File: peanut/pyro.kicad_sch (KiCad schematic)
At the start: 16 parts, among them J2 PYRO_OUT, Q2 NMOS, Q3 NMOS, Q4 NMOS

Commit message: bug: Fix arming flaw
Fixed the arming circuitry so that the ARM terminal prevents power going
to the pyro channels. This means that the rest of the board can be
powered on before arming, which is good because:

- It allows configuring without arming
- Software arming can still be done as a second stage
- The MCU can be in low-power mode until told to arm over BLE
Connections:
- net VBAT_RAW renamed VPYRO
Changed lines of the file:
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@@
 		(in_pos_files yes)
 		(dnp no)
-		(fields_autoplaced yes)
 		(property "Reference" "#PWR058"
 			(at 196.85 93.98 0)
@@
 			)
 		)
-		(property "Value" "VBAT_RAW"
-			(at 196.85 85.09 0)
-			(show_name no)
-			(do_not_autoplace no)
-			(effects
-				(font
-					(size 1.27 1.27)
-				)
+		(property "Value" "VPYRO"
+			(at 194.056 85.598 0)
+			(show_name no)
+			(do_not_autoplace no)
+			(effects
+				(font
+					(size 1.27 1.27)
+				)
+				(justify left)
 			)
 		)
@@
 		(in_pos_files yes)
 		(dnp no)
-		(fields_autoplaced yes)
 		(property "Reference" "#PWR057"
 			(at 156.21 93.98 0)
@@
 			)
 		)
-		(property "Value" "VBAT_RAW"
-			(at 156.21 85.09 0)
-			(show_name no)
-			(do_not_autoplace no)
-			(effects
-				(font
-					(size 1.27 1.27)
-				)
-			)
-		)
+		(property "Value" "VPYRO"
+			(at 153.67 85.598 0)
+			(show_name no)
+			(do_not_autoplace no)
+			(effects
+				(font
+					(size 1.27 1.27)
+				)
+				(justify left)
+			)
+		)

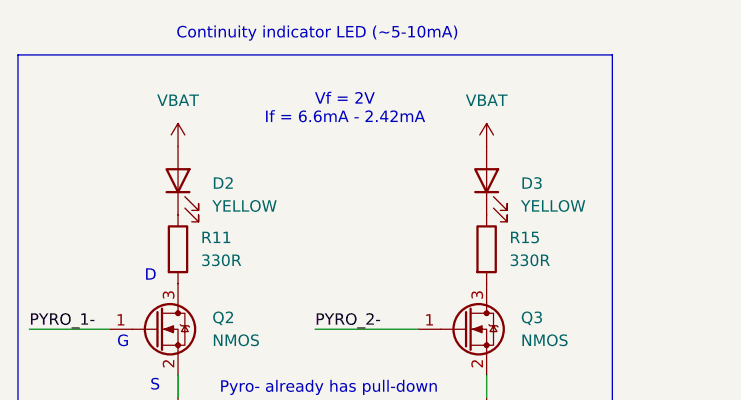
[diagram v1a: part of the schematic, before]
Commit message: chore: Clean up routing
Cleaned up some traces and added teardrops.
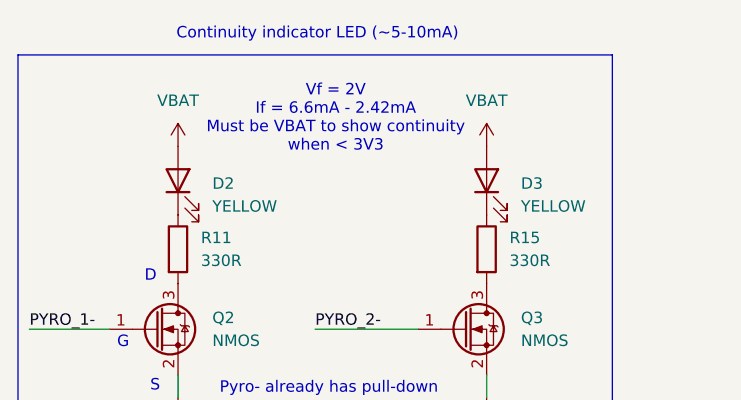
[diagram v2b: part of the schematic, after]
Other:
- note added: "Vf = 2V If = 6.6mA - 2.42mA Must be VBAT to show continuity when < 3V3"
- note removed: "Vf = 2V If = 6.6mA - 2.42mA"
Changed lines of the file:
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@@
 		)
 	)
-	(text "Vf = 2V\nIf = 6.6mA - 2.42mA"
+	(text "Vf = 2V\nIf = 6.6mA - 2.42mA\nMust be VBAT to show continuity\nwhen < 3V3"
 		(exclude_from_sim no)
-		(at 69.342 88.646 0)
+		(at 68.326 89.662 0)
 		(effects
 			(font

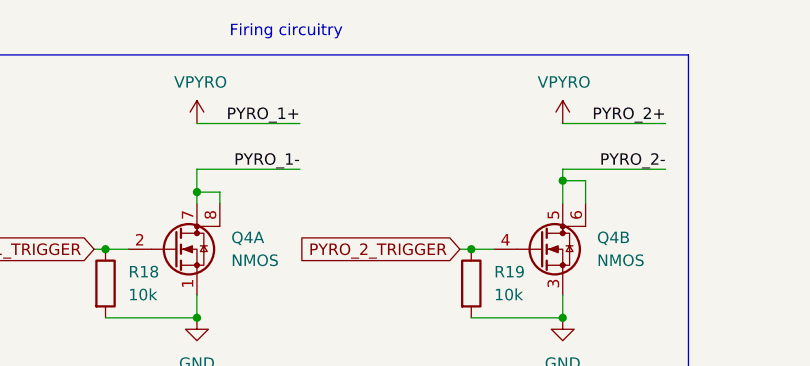
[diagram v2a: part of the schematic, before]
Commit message: feat: Better arming circuit
Improved the arming circuit connections so that both circuits are
powered off until armed.

Signed-off-by: Matteo Golin <matteo.golin@gmail.com>
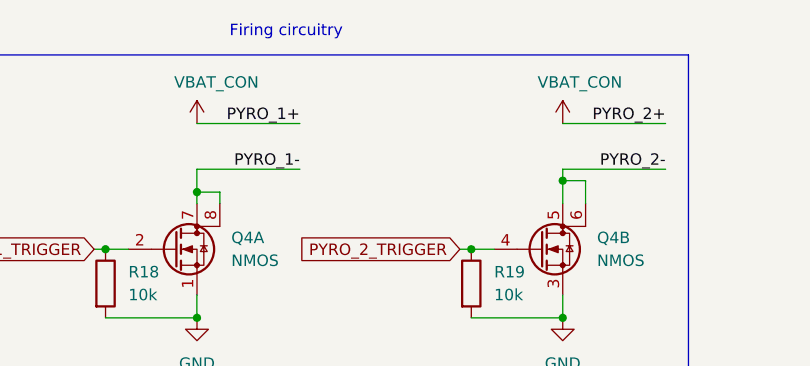
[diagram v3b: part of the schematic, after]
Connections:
- net VPYRO renamed VBAT_CON
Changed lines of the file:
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@@
 			)
 		)
-		(property "Value" "VPYRO"
+		(property "Value" "VBAT_CON"
 			(at 194.056 85.598 0)
 			(show_name no)
@@
 			)
 		)
-		(property "Value" "VPYRO"
+		(property "Value" "VBAT_CON"
 			(at 153.67 85.598 0)
 			(show_name no)

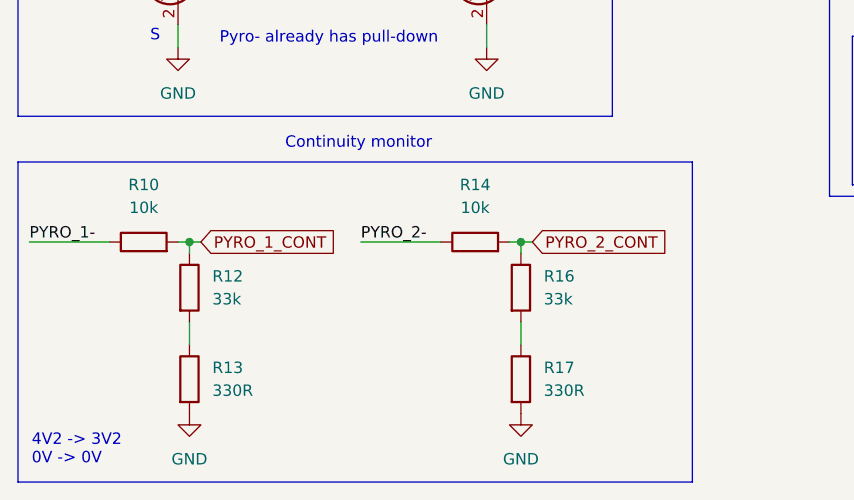
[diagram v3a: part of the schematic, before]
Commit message: Fix ADC voltage monitoring to use 1:1 ratio
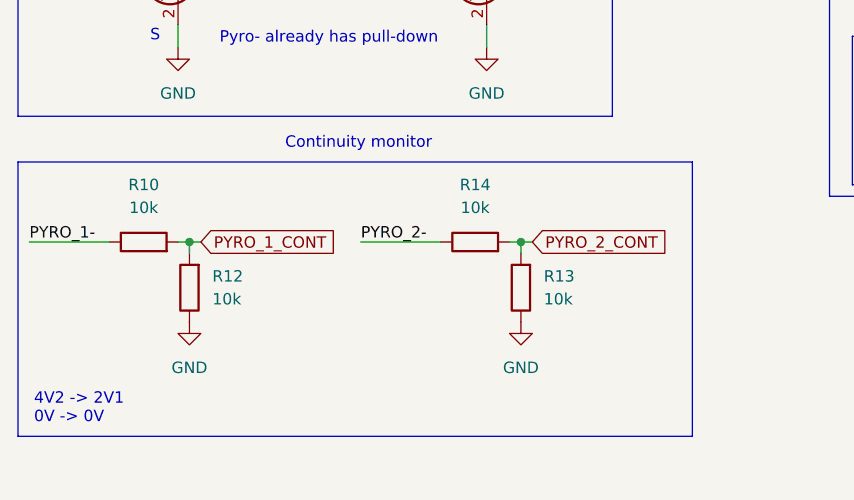
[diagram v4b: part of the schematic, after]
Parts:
- removed R16: 33k, Resistor_SMD:R_0402_1005Metric, symbol Device:R
- removed R17: 330R, Resistor_SMD:R_0402_1005Metric, symbol Device:R
- R12: value 33k -> 10k; MPN MR04X3302FTL -> MCS04020C1002FE000
- R13: value 330R -> 10k; MPN 560112110231 -> MCS04020C1002FE000
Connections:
- net GND: now also R12.1, R13.1; no longer R13.2
- net PYRO_1_CONT: now also R12.2; no longer R12.1
- net PYRO_2_CONT: now also R13.2
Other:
- note added: "4V2 -> 2V1 0V -> 0V"
- note removed: "4V2 -> 3V2 0V -> 0V"

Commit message: chore: re-annotate
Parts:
- renumbered D2 to D3, D3 to D4, R10 to R12, R11 to R13, R12 to R14, R14 to R15, R15 to R16, R13 to R17
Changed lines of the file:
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@@
 		(dnp no)
 		(fields_autoplaced yes)
-		(property "Reference" "#PWR038"
+		(property "Reference" "#PWR040"
 			(at 196.85 118.11 0)
 			(hide yes)
@@
 			(project "peanut"
 				(path "/5c6b6cfc-6c84-425a-9b66-e6111713aae8/4be069cc-6620-4cc3-a173-eaa174b1ef03"
-					(reference "#PWR038")
+					(reference "#PWR040")
 					(unit 1)
 				)
@@
 		(dnp no)
 		(fields_autoplaced yes)
-		(property "Reference" "R13"
+		(property "Reference" "R17"
 			(at 91.44 146.0499 0)
 			(show_name no)
@@
 			(project "peanut"
 				(path "/5c6b6cfc-6c84-425a-9b66-e6111713aae8/4be069cc-6620-4cc3-a173-eaa174b1ef03"
-					(reference "R13")
+					(reference "R17")
 					(unit 1)
 				)
@@
 		(in_pos_files yes)
 		(dnp no)
-		(property "Reference" "#PWR058"
+		(property "Reference" "#PWR039"
 			(at 196.85 93.98 0)
 			(hide yes)
@@
 			(project "peanut"
 				(path "/5c6b6cfc-6c84-425a-9b66-e6111713aae8/4be069cc-6620-4cc3-a173-eaa174b1ef03"
-					(reference "#PWR058")
+					(reference "#PWR039")
 					(unit 1)
 				)
@@
 		(dnp no)
 		(fields_autoplaced yes)
-		(property "Reference" "R12"
+		(property "Reference" "R14"
 			(at 54.61 146.0499 0)
 			(show_name no)
@@
 			(project "peanut"
 				(path "/5c6b6cfc-6c84-425a-9b66-e6111713aae8/4be069cc-6620-4cc3-a173-eaa174b1ef03"
-					(reference "R12")
+					(reference "R14")
 					(unit 1)
 				)
@@
 		(dnp no)
 		(fields_autoplaced yes)
-		(property "Reference" "D3"
+		(property "Reference" "D4"
 			(at 88.9 96.8374 90)
 			(show_name no)
@@
 			(project "peanut"
 				(path "/5c6b6cfc-6c84-425a-9b66-e6111713aae8/4be069cc-6620-4cc3-a173-eaa174b1ef03"
-					(reference "D3")
+					(reference "D4")
 					(unit 1)
 				)
@@
 		(dnp no)
 		(fields_autoplaced yes)
-		(property "Reference" "#PWR036"
+		(property "Reference" "#PWR038"
 			(at 156.21 118.11 0)
 			(hide yes)
@@
 			(project "peanut"
 				(path "/5c6b6cfc-6c84-425a-9b66-e6111713aae8/4be069cc-6620-4cc3-a173-eaa174b1ef03"
-					(reference "#PWR036")
+					(reference "#PWR038")
 					(unit 1)
 				)
@@
 		(dnp no)
 		(fields_autoplaced yes)
-		(property "Reference" "R15"
+		(property "Reference" "R16"
 			(at 87.63 102.8699 0)
 			(show_name no)
@@
 			(project "peanut"
 				(path "/5c6b6cfc-6c84-425a-9b66-e6111713aae8/4be069cc-6620-4cc3-a173-eaa174b1ef03"
-					(reference "R15")
+					(reference "R16")
 					(unit 1)
 				)
@@
 		(dnp no)
 		(fields_autoplaced yes)
-		(property "Reference" "#PWR030"
+		(property "Reference" "#PWR032"
 			(at 50.8 127 0)
 			(hide yes)
@@
 			(project "peanut"
 				(path "/5c6b6cfc-6c84-425a-9b66-e6111713aae8/4be069cc-6620-4cc3-a173-eaa174b1ef03"
-					(reference "#PWR030")
+					(reference "#PWR032")
 					(unit 1)
 				)
@@
 		(dnp no)
 		(fields_autoplaced yes)
-		(property "Reference" "#PWR033"
+		(property "Reference" "#PWR035"
 			(at 85.09 127 0)
 			(hide yes)
@@
 			(project "peanut"
 				(path "/5c6b6cfc-6c84-425a-9b66-e6111713aae8/4be069cc-6620-4cc3-a173-eaa174b1ef03"
-					(reference "#PWR033")
+					(reference "#PWR035")
 					(unit 1)
 				)
@@
 		(dnp no)
 		(fields_autoplaced yes)
-		(property "Reference" "#PWR034"
+		(property "Reference" "#PWR036"
 			(at 88.9 157.48 0)
 			(hide yes)
@@
 			(project "peanut"
 				(path "/5c6b6cfc-6c84-425a-9b66-e6111713aae8/4be069cc-6620-4cc3-a173-eaa174b1ef03"
-					(reference "#PWR034")
+					(reference "#PWR036")
 					(unit 1)
 				)
@@
 		(dnp no)
 		(fields_autoplaced yes)
-		(property "Reference" "D2"
+		(property "Reference" "D3"
 			(at 54.61 96.8374 90)
 			(show_name no)
@@
 			(project "peanut"
 				(path "/5c6b6cfc-6c84-425a-9b66-e6111713aae8/4be069cc-6620-4cc3-a173-eaa174b1ef03"
-					(reference "D2")
+					(reference "D3")
 					(unit 1)
 				)
@@
 		(dnp no)
 		(fields_autoplaced yes)
-		(property "Reference" "#PWR031"
+		(property "Reference" "#PWR033"
 			(at 52.07 157.48 0)
 			(hide yes)
@@
 			(project "peanut"
 				(path "/5c6b6cfc-6c84-425a-9b66-e6111713aae8/4be069cc-6620-4cc3-a173-eaa174b1ef03"
-					(reference "#PWR031")
+					(reference "#PWR033")
 					(unit 1)
 				)
@@
 		(dnp no)
 		(fields_autoplaced yes)
-		(property "Reference" "R14"
+		(property "Reference" "R15"
 			(at 83.82 135.89 90)
 			(show_name no)
@@
 			(project "peanut"
 				(path "/5c6b6cfc-6c84-425a-9b66-e6111713aae8/4be069cc-6620-4cc3-a173-eaa174b1ef03"
-					(reference "R14")
+					(reference "R15")
 					(unit 1)
 				)
@@
 		(in_pos_files yes)
 		(dnp no)
-		(property "Reference" "#PWR057"
+		(property "Reference" "#PWR037"
 			(at 156.21 93.98 0)
 			(hide yes)
@@
 			(project "peanut"
 				(path "/5c6b6cfc-6c84-425a-9b66-e6111713aae8/4be069cc-6620-4cc3-a173-eaa174b1ef03"
-					(reference "#PWR057")
+					(reference "#PWR037")
 					(unit 1)
 				)
@@
 		(dnp no)
 		(fields_autoplaced yes)
-		(property "Reference" "#PWR029"
+		(property "Reference" "#PWR031"
 			(at 50.8 96.52 0)
 			(hide yes)
@@
 			(project "peanut"
 				(path "/5c6b6cfc-6c84-425a-9b66-e6111713aae8/4be069cc-6620-4cc3-a173-eaa174b1ef03"
-					(reference "#PWR029")
+					(reference "#PWR031")
 					(unit 1)
 				)
@@
 		(dnp no)
 		(fields_autoplaced yes)
-		(property "Reference" "#PWR032"
+		(property "Reference" "#PWR034"
 			(at 85.09 96.52 0)
 			(hide yes)
@@
 			(project "peanut"
 				(path "/5c6b6cfc-6c84-425a-9b66-e6111713aae8/4be069cc-6620-4cc3-a173-eaa174b1ef03"
-					(reference "#PWR032")
+					(reference "#PWR034")
 					(unit 1)
 				)
@@
 		(dnp no)
 		(fields_autoplaced yes)
-		(property "Reference" "R10"
+		(property "Reference" "R12"
 			(at 46.99 135.89 90)
 			(show_name no)
@@
 			(project "peanut"
 				(path "/5c6b6cfc-6c84-425a-9b66-e6111713aae8/4be069cc-6620-4cc3-a173-eaa174b1ef03"
-					(reference "R10")
+					(reference "R12")
 					(unit 1)
 				)
@@
 		(dnp no)
 		(fields_autoplaced yes)
-		(property "Reference" "R11"
+		(property "Reference" "R13"
 			(at 53.34 102.8699 0)
 			(show_name no)
@@
 			(project "peanut"
 				(path "/5c6b6cfc-6c84-425a-9b66-e6111713aae8/4be069cc-6620-4cc3-a173-eaa174b1ef03"
-					(reference "R11")
-					(unit 1)
-				)
+					(reference "R13")
+					(unit 1)
+				)
